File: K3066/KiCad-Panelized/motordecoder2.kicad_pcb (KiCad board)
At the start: 2 copper layers, 76 x 98 mm, 600 parts, among them J11 PAD, J12 PAD, J14 PAD, J16 PAD, J18 PAD, J19 PAD, P1 PAD, P10 PAD, P11 PAD, P2 PAD, P3 PAD, P4 PAD, P5 PAD, P6 PAD, P7 PAD, P8 PAD, P9 PROG, Q1 DMG6601LVT, Q11 SSM3K7002BFU, Q12 SSM6N7002BFE, Q13 SSM6N7002BFE, Q14 SSM6N7002BFE, Q2 DMG6601LVT, Q21 PMBT3906VS, Q22 SSM6N7002BFE, Q3 PMBT3904VS, Q5 2SC4116, Q6 PMBT3906VS, Q8 PMBT3904VS, U2 ATtiny1606-M

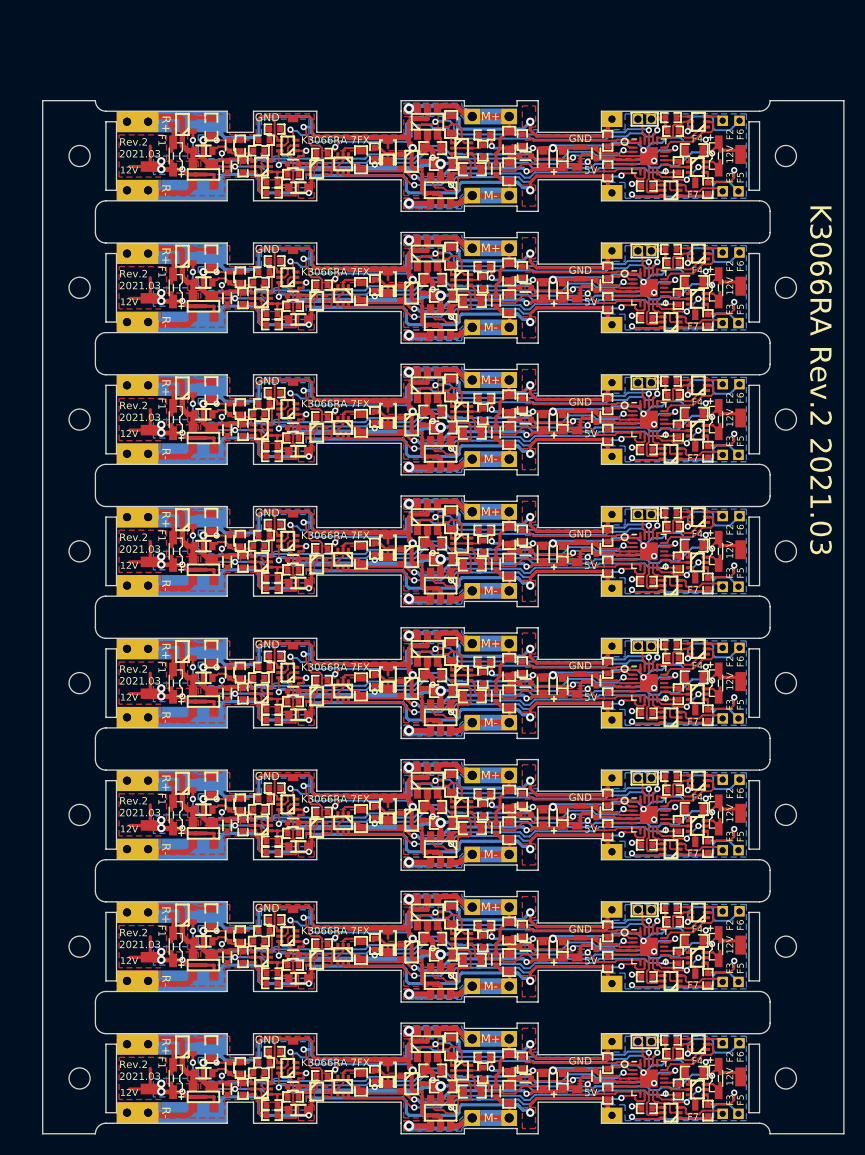
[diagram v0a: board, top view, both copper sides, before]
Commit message: 回路の問題点を修正 (K3066: Rev3 / それ以外: Rev2)
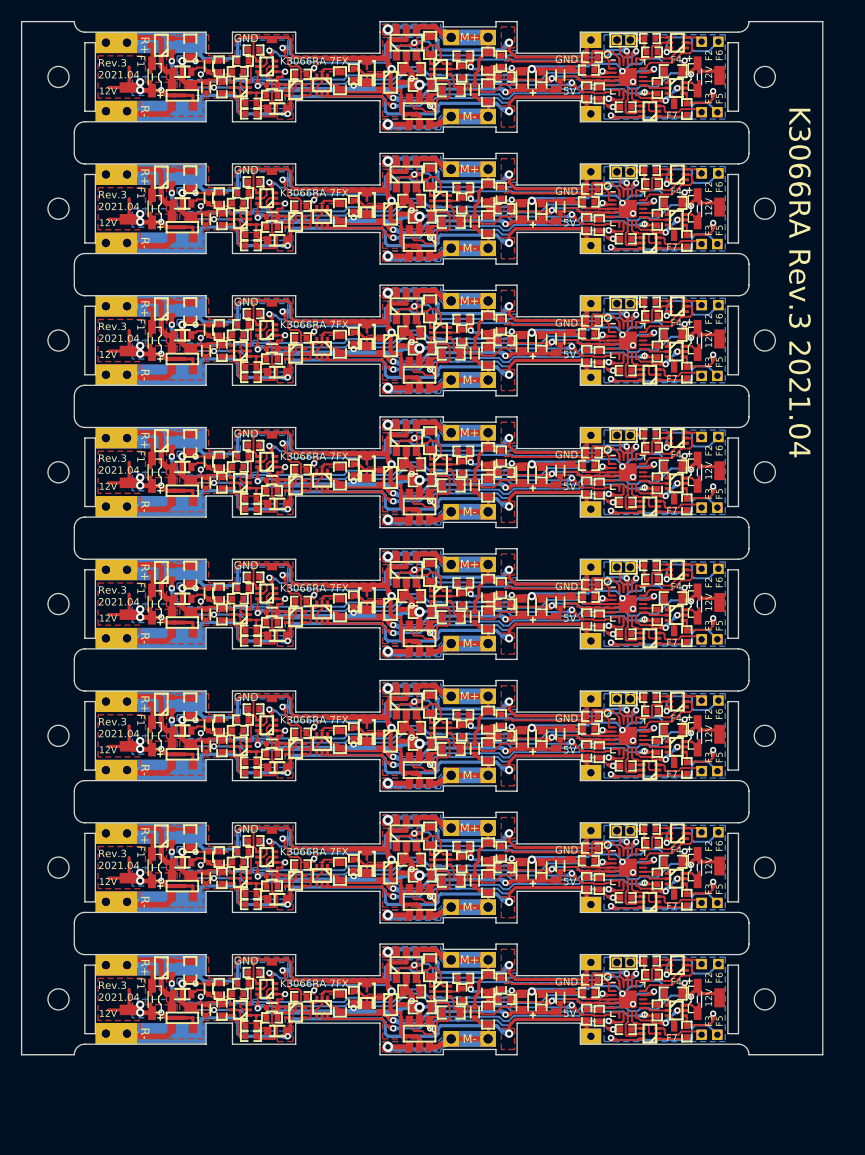
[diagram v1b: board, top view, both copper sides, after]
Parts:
- removed the C1 at (127.5, 138.8)
- removed the C1 at (127.5, 126.2)
- removed the C1 at (127.5, 113.8)
- removed the C1 at (127.5, 101.2)
- removed the C1 at (127.5, 88.8)
- removed the C1 at (127.5, 76.2)
- removed the C1 at (127.5, 63.8)
- removed the C11 at (127.8, 136.8)
- removed the C11 at (127.8, 124.2)
- removed the C11 at (127.8, 111.8)
- removed the C11 at (127.8, 99.2)
- removed the C11 at (127.8, 86.8)
- removed the C11 at (127.8, 74.2)
- removed the C11 at (127.8, 61.8)
- removed the C12 at (133.8, 138.5)
- removed the C12 at (133.8, 126.0)
- removed the C12 at (133.8, 113.5)
- removed the C12 at (133.8, 101.0)
- removed the C12 at (133.8, 88.5)
- removed the C12 at (133.8, 76.0)
- removed the C12 at (133.8, 63.5)
- removed the C3 at (157.5, 138.0)
- removed the C3 at (157.5, 125.5)
- removed the C3 at (157.5, 113.0)
- removed the C3 at (157.5, 100.5)
- removed the C3 at (157.5, 88.0)
- removed the C3 at (157.5, 75.5)
- removed the C3 at (157.5, 63.0)
- removed the C4 at (159.3, 138.0)
- removed the C4 at (159.3, 125.5)
- removed the C4 at (159.3, 113.0)
- removed the C4 at (159.3, 100.5)
- removed the C4 at (159.3, 88.0)
- removed the C4 at (159.3, 75.5)
- removed the C4 at (159.3, 63.0)
- removed the C5 at (162.5, 137.5)
- removed the C5 at (162.5, 125.0)
- removed the C5 at (162.5, 112.5)
- removed the C5 at (162.5, 100.0)
- removed the C5 at (162.5, 87.5)
- removed the C5 at (162.5, 75.0)
- removed the C5 at (162.5, 62.5)
- removed C6 (x8): 104, footprint:C_1005_v2
- removed the C7 at (153.0, 139.0)
- removed the C7 at (153.0, 126.5)
- removed the C7 at (153.0, 114.0)
- removed the C7 at (153.0, 101.5)
- removed the C7 at (153.0, 89.0)
- removed the C7 at (153.0, 76.5)
- removed the C7 at (153.0, 64.0)
- removed the D1 at (125.2, 139.5)
- removed the D1 at (125.2, 127.0)
- removed the D1 at (125.2, 114.5)
- removed the D1 at (125.2, 102.0)
- removed the D1 at (125.2, 89.5)
- removed the D1 at (125.2, 77.0)
- removed the D1 at (125.2, 64.5)
- removed the D11 at (122.0, 137.8)
- removed the D11 at (122.0, 125.2)
- removed the D11 at (122.0, 112.8)
- removed the D11 at (122.0, 100.2)
- removed the D11 at (122.0, 87.8)
- removed the D11 at (122.0, 75.2)
- removed the D11 at (122.0, 62.8)
- removed the D12 at (174.5, 137.8)
- removed the D12 at (174.5, 125.2)
- removed the D12 at (174.5, 112.8)
- removed the D12 at (174.5, 100.2)
- removed the D12 at (174.5, 87.8)
- removed the D12 at (174.5, 75.2)
- removed the D12 at (174.5, 62.8)
- removed the D21 at (125.2, 137.2)
- removed the D21 at (125.2, 124.8)
- removed the D21 at (125.2, 112.2)
- removed the D21 at (125.2, 99.8)
- removed the D21 at (125.2, 87.2)
- removed the D21 at (125.2, 74.8)
- removed the D21 at (125.2, 62.2)
- removed the D22 at (134.2, 140.8)
- removed the D22 at (134.2, 128.2)
- removed the D22 at (134.2, 115.8)
- removed the D22 at (134.2, 103.2)
- removed the D22 at (134.2, 90.8)
- removed the D22 at (134.2, 78.2)
- removed the D22 at (134.2, 65.8)
- removed the D3 at (142.8, 137.2)
- removed the D3 at (142.8, 124.8)
- removed the D3 at (142.8, 112.2)
- removed the D3 at (142.8, 99.8)
- removed the D3 at (142.8, 87.2)
- removed the D3 at (142.8, 74.8)
- removed the D3 at (142.8, 62.2)
- removed the J11 at (176.2, 137.6)
- removed the J11 at (176.2, 125.1)
- removed the J11 at (176.2, 112.6)
- removed the J11 at (176.2, 100.1)
- removed the J11 at (176.2, 87.6)
- removed the J11 at (176.2, 75.1)
- removed the J11 at (176.2, 62.6)
- removed the J12 at (176.0, 141.1)
- removed the J12 at (176.0, 128.6)
- removed the J12 at (176.0, 116.1)
- removed the J12 at (176.0, 103.6)
- removed the J12 at (176.0, 91.1)
- removed the J12 at (176.0, 78.6)
- removed the J12 at (176.0, 66.1)
- removed the J14 at (174.5, 141.1)
- removed the J14 at (174.5, 128.6)
- removed the J14 at (174.5, 116.1)
- removed the J14 at (174.5, 103.6)
- removed the J14 at (174.5, 91.1)
- removed the J14 at (174.5, 78.6)
- removed the J14 at (174.5, 66.1)
- removed the J16 at (176.1, 134.4)
- removed the J16 at (176.1, 121.9)
- removed the J16 at (176.1, 109.4)
- removed the J16 at (176.1, 96.9)
- removed the J16 at (176.1, 84.4)
- removed the J16 at (176.1, 71.9)
- removed the J16 at (176.1, 59.4)
- removed the J18 at (174.5, 134.4)
- removed the J18 at (174.5, 121.9)
- removed the J18 at (174.5, 109.4)
- removed the J18 at (174.5, 96.9)
- removed the J18 at (174.5, 84.4)
- removed the J18 at (174.5, 71.9)
- removed the J18 at (174.5, 59.4)
- removed the J19 at (171.9, 140.3)
- removed the J19 at (171.9, 127.8)
- removed the J19 at (171.9, 115.3)
- removed the J19 at (171.9, 102.8)
- removed the J19 at (171.9, 90.3)
- removed the J19 at (171.9, 77.8)
- removed the J19 at (171.9, 65.3)
- removed the P1 at (119.0, 134.5)
- removed the P1 at (119.0, 122.0)
- removed the P1 at (119.0, 109.5)
- removed the P1 at (119.0, 97.0)
- removed the P1 at (119.0, 84.5)
- removed the P1 at (119.0, 72.0)
- removed the P1 at (119.0, 59.5)
- removed the P10 at (160.7, 138.8)
- removed the P10 at (160.7, 126.3)
- removed the P10 at (160.7, 113.8)
- removed the P10 at (160.7, 101.3)
- removed the P10 at (160.7, 88.8)
- removed the P10 at (160.7, 76.3)
- removed the P10 at (160.7, 63.9)
- removed the P11 at (161.0, 136.9)
- removed the P11 at (161.0, 124.4)
- removed the P11 at (161.0, 111.9)
- removed the P11 at (161.0, 99.4)
- removed the P11 at (161.0, 86.9)
- removed the P11 at (161.0, 74.4)
- removed the P11 at (161.0, 61.9)
- removed the P11 at (161.0, 49.4)
- removed the P2 at (164.0, 134.2)
- removed the P2 at (164.0, 121.8)
- removed the P2 at (164.0, 109.2)
- removed the P2 at (164.0, 96.8)
- removed the P2 at (164.0, 84.2)
- removed the P2 at (164.0, 71.8)
- removed the P2 at (164.0, 59.2)
- removed the P3 at (119.0, 141.0)
- removed the P3 at (119.0, 128.5)
- removed the P3 at (119.0, 116.0)
- removed the P3 at (119.0, 103.5)
- removed the P3 at (119.0, 91.0)
- removed the P3 at (119.0, 78.5)
- removed the P3 at (119.0, 66.0)
- removed the P4 at (164.0, 141.2)
- removed the P4 at (164.0, 128.8)
- removed the P4 at (164.0, 116.2)
- removed the P4 at (164.0, 103.8)
- removed the P4 at (164.0, 91.2)
- removed the P4 at (164.0, 78.8)
- removed the P4 at (164.0, 66.2)
- removed the P5 at (152.5, 134.0)
- removed the P5 at (152.5, 121.5)
- removed the P5 at (152.5, 109.0)
- removed the P5 at (152.5, 96.5)
- removed the P5 at (152.5, 84.0)
- removed the P5 at (152.5, 71.5)
- removed the P5 at (152.5, 59.0)
- removed the P6 at (152.5, 141.5)
- removed the P6 at (152.5, 129.0)
- removed the P6 at (152.5, 116.5)
- removed the P6 at (152.5, 104.0)
- removed the P6 at (152.5, 91.5)
- removed the P6 at (152.5, 79.0)
- removed the P6 at (152.5, 66.5)
- removed the P7 at (120.2, 138.8)
- removed the P7 at (120.2, 126.2)
- removed the P7 at (120.2, 113.8)
- removed the P7 at (120.2, 101.2)
- removed the P7 at (120.2, 88.8)
- removed the P7 at (120.2, 76.2)
- removed the P7 at (120.2, 63.8)
- removed the P8 at (133.8, 134.2)
- removed the P8 at (133.8, 121.8)
- removed the P8 at (133.8, 109.2)
- removed the P8 at (133.8, 96.8)
- removed the P8 at (133.8, 84.2)
- removed the P8 at (133.8, 71.8)
- removed the P8 at (133.8, 59.2)
- removed the P9 at (167.1, 134.2)
- removed the P9 at (167.1, 121.8)
- removed the P9 at (167.1, 109.2)
- removed the P9 at (167.1, 96.8)
- removed the P9 at (167.1, 84.2)
- removed the P9 at (167.1, 71.8)
- removed the P9 at (167.1, 59.2)
- removed the Q1 at (146.5, 134.5)
- removed the Q1 at (146.5, 122.0)
- removed the Q1 at (146.5, 109.5)
- removed the Q1 at (146.5, 97.0)
- removed the Q1 at (146.5, 84.5)
- removed the Q1 at (146.5, 72.0)
- removed the Q1 at (146.5, 59.5)
- removed the Q11 at (123.2, 134.8)
- removed the Q11 at (123.2, 122.2)
- removed the Q11 at (123.2, 109.8)
- removed the Q11 at (123.2, 97.2)
- removed the Q11 at (123.2, 84.8)
- removed the Q11 at (123.2, 72.2)
- removed the Q11 at (123.2, 59.8)
- removed the Q12 at (172.1, 138.8)
- removed the Q12 at (172.1, 126.3)
- removed the Q12 at (172.1, 113.8)
- removed the Q12 at (172.1, 101.3)
- removed the Q12 at (172.1, 88.8)
- removed the Q12 at (172.1, 76.3)
- removed the Q12 at (172.1, 63.8)
- removed the Q13 at (169.6, 141.0)
- removed the Q13 at (169.6, 128.5)
- removed the Q13 at (169.6, 116.0)
- removed the Q13 at (169.6, 103.5)
- removed the Q13 at (169.6, 91.0)
- removed the Q13 at (169.6, 78.5)
- removed the Q13 at (169.6, 66.0)
- removed the Q14 at (172.2, 134.5)
- removed the Q14 at (172.2, 122.0)
- removed the Q14 at (172.2, 109.5)
- removed the Q14 at (172.2, 97.0)
- removed the Q14 at (172.2, 84.5)
- removed the Q14 at (172.2, 72.0)
- removed the Q14 at (172.2, 59.5)
- removed the Q2 at (147.8, 141.0)
- removed the Q2 at (147.8, 128.5)
- removed the Q2 at (147.8, 116.0)
- removed the Q2 at (147.8, 103.5)
- removed the Q2 at (147.8, 91.0)
- removed the Q2 at (147.8, 78.5)
- removed the Q2 at (147.8, 66.0)
- removed the Q21 at (130.8, 138.8)
- removed the Q21 at (130.8, 126.2)
- removed the Q21 at (130.8, 113.8)
- removed the Q21 at (130.8, 101.2)
- removed the Q21 at (130.8, 88.8)
- removed the Q21 at (130.8, 76.2)
- removed the Q21 at (130.8, 63.8)
- removed the Q22 at (133.2, 136.8)
- removed the Q22 at (133.2, 124.2)
- removed the Q22 at (133.2, 111.8)
- removed the Q22 at (133.2, 99.2)
- removed the Q22 at (133.2, 86.8)
- removed the Q22 at (133.2, 74.2)
- removed the Q22 at (133.2, 61.8)
- removed the Q3 at (149.8, 137.0)
- removed the Q3 at (149.8, 124.5)
- removed the Q3 at (149.8, 112.0)
- removed the Q3 at (149.8, 99.5)
- removed the Q3 at (149.8, 87.0)
- removed the Q3 at (149.8, 74.5)
- removed the Q3 at (149.8, 62.0)
- removed the Q5 at (145.0, 138.2)
- removed the Q5 at (145.0, 125.8)
- removed the Q5 at (145.0, 113.2)
- removed the Q5 at (145.0, 100.8)
- removed the Q5 at (145.0, 88.2)
- removed the Q5 at (145.0, 75.8)
- removed the Q5 at (145.0, 63.2)
- removed the Q6 at (138.5, 138.5)
- removed the Q6 at (138.5, 126.0)
- removed the Q6 at (138.5, 113.5)
- removed the Q6 at (138.5, 101.0)
- removed the Q6 at (138.5, 88.5)
- removed the Q6 at (138.5, 76.0)
- removed the Q6 at (138.5, 63.5)
- removed the Q8 at (136.0, 139.0)
- removed the Q8 at (136.0, 126.5)
- removed the Q8 at (136.0, 114.0)
- removed the Q8 at (136.0, 101.5)
- removed the Q8 at (136.0, 89.0)
- removed the Q8 at (136.0, 76.5)
- removed the Q8 at (136.0, 64.0)
- removed the R1 at (163.6, 136.3)
- removed the R1 at (163.6, 123.8)
- removed the R1 at (163.6, 111.3)
- removed the R1 at (163.6, 98.8)
- removed the R1 at (163.6, 86.3)
- removed the R1 at (163.6, 73.8)
- removed the R1 at (163.6, 61.3)
- removed the R1 at (163.6, 48.8)
- removed the R10 at (154.2, 139.2)
- removed the R10 at (154.2, 126.8)
- removed the R10 at (154.2, 114.2)
- removed the R10 at (154.2, 101.8)
- removed the R10 at (154.2, 89.2)
- removed the R10 at (154.2, 76.8)
- removed the R10 at (154.2, 64.2)
- removed the R11 at (155.5, 136.2)
- removed the R11 at (155.5, 123.8)
- removed the R11 at (155.5, 111.2)
- removed the R11 at (155.5, 98.8)
- removed the R11 at (155.5, 86.2)
- removed the R11 at (155.5, 73.8)
- removed the R11 at (155.5, 61.2)
- removed the R12 at (141.5, 137.5)
- removed the R12 at (141.5, 125.0)
- removed the R12 at (141.5, 112.5)
- removed the R12 at (141.5, 100.0)
- removed the R12 at (141.5, 87.5)
- removed the R12 at (141.5, 75.0)
- removed the R12 at (141.5, 62.5)
- removed the R13 at (170.3, 138.8)
- removed the R13 at (170.3, 126.3)
- removed the R13 at (170.3, 113.8)
- removed the R13 at (170.3, 101.3)
- removed the R13 at (170.3, 88.8)
- removed the R13 at (170.3, 76.3)
- removed the R13 at (170.3, 63.8)
- removed the R14 at (140.2, 138.1)
- removed the R14 at (140.2, 125.6)
- removed the R14 at (140.2, 113.1)
- removed the R14 at (140.2, 100.6)
- removed the R14 at (140.2, 88.1)
- removed the R14 at (140.2, 75.6)
- removed the R14 at (140.2, 63.1)
- removed the R15 at (136.5, 137.5)
- removed the R15 at (136.5, 125.0)
- removed the R15 at (136.5, 112.5)
- removed the R15 at (136.5, 100.0)
- removed the R15 at (136.5, 87.5)
- removed the R15 at (136.5, 75.0)
- removed the R15 at (136.5, 62.5)
- removed the R2 at (163.6, 139.2)
- removed the R2 at (163.6, 126.7)
- removed the R2 at (163.6, 114.2)
- removed the R2 at (163.6, 101.7)
- removed the R2 at (163.6, 89.2)
- removed the R2 at (163.6, 76.7)
- removed the R2 at (163.6, 64.2)
- removed the R21 at (126.0, 135.0)
- removed the R21 at (126.0, 122.5)
- removed the R21 at (126.0, 110.0)
- removed the R21 at (126.0, 97.5)
- removed the R21 at (126.0, 85.0)
- removed the R21 at (126.0, 72.5)
- removed the R21 at (126.0, 60.0)
- removed the R22 at (171.8, 137.2)
- removed the R22 at (171.8, 124.7)
- removed the R22 at (171.8, 112.2)
- removed the R22 at (171.8, 99.7)
- removed the R22 at (171.8, 87.2)
- removed the R22 at (171.8, 74.7)
- removed the R22 at (171.8, 62.2)
- removed the R23 at (173.1, 140.8)
- removed the R23 at (173.1, 128.3)
- removed the R23 at (173.1, 115.8)
- removed the R23 at (173.1, 103.3)
- removed the R23 at (173.1, 90.8)
- removed the R23 at (173.1, 78.3)
- removed the R23 at (173.1, 65.8)
- removed the R24 at (167.3, 140.6)
- removed the R24 at (167.3, 128.1)
- removed the R24 at (167.3, 115.6)
- removed the R24 at (167.3, 103.1)
- removed the R24 at (167.3, 90.6)
- removed the R24 at (167.3, 78.1)
- removed the R24 at (167.3, 65.6)
- removed the R25 at (169.8, 135.4)
- removed the R25 at (169.8, 122.9)
- removed the R25 at (169.8, 110.4)
- removed the R25 at (169.8, 97.9)
- removed the R25 at (169.8, 85.4)
- removed the R25 at (169.8, 72.9)
- removed the R25 at (169.8, 60.4)
- removed the R26 at (169.6, 134.1)
- removed the R26 at (169.6, 121.6)
- removed the R26 at (169.6, 109.1)
- removed the R26 at (169.6, 96.6)
- removed the R26 at (169.6, 84.1)
- removed the R26 at (169.6, 71.6)
- removed the R26 at (169.6, 59.1)
- removed the R3 at (147.0, 137.0)
- removed the R3 at (147.0, 124.5)
- removed the R3 at (147.0, 112.0)
- removed the R3 at (147.0, 99.5)
- removed the R3 at (147.0, 87.0)
- removed the R3 at (147.0, 74.5)
- removed the R3 at (147.0, 62.0)
- removed the R31 at (130.5, 137.2)
- removed the R31 at (130.5, 124.8)
- removed the R31 at (130.5, 112.2)
- removed the R31 at (130.5, 99.8)
- removed the R31 at (130.5, 87.2)
- removed the R31 at (130.5, 74.8)
- removed the R31 at (130.5, 62.2)
- removed the R32 at (128.8, 136.8)
- removed the R32 at (128.8, 124.2)
- removed the R32 at (128.8, 111.8)
- removed the R32 at (128.8, 99.2)
- removed the R32 at (128.8, 86.8)
- removed the R32 at (128.8, 74.2)
- removed the R32 at (128.8, 61.8)
- removed the R33 at (129.0, 138.8)
- removed the R33 at (129.0, 126.2)
- removed the R33 at (129.0, 113.8)
- removed the R33 at (129.0, 101.2)
- removed the R33 at (129.0, 88.8)
- removed the R33 at (129.0, 76.2)
- removed the R33 at (129.0, 63.8)
- removed the R34 at (131.8, 141.2)
- removed the R34 at (131.8, 128.8)
- removed the R34 at (131.8, 116.2)
- removed the R34 at (131.8, 103.8)
- removed the R34 at (131.8, 91.2)
- removed the R34 at (131.8, 78.8)
- removed the R34 at (131.8, 66.2)
- removed the R35 at (131.8, 140.2)
- removed the R35 at (131.8, 127.8)
- removed the R35 at (131.8, 115.2)
- removed the R35 at (131.8, 102.8)
- removed the R35 at (131.8, 90.2)
- removed the R35 at (131.8, 77.8)
- removed the R35 at (131.8, 65.2)
- removed the R36 at (133.8, 139.5)
- removed the R36 at (133.8, 127.0)
- removed the R36 at (133.8, 114.5)
- removed the R36 at (133.8, 102.0)
- removed the R36 at (133.8, 89.5)
- removed the R36 at (133.8, 77.0)
- removed the R36 at (133.8, 64.5)
- removed the R37 at (131.0, 136.2)
- removed the R37 at (131.0, 123.8)
- removed the R37 at (131.0, 111.2)
- removed the R37 at (131.0, 98.8)
- removed the R37 at (131.0, 86.2)
- removed the R37 at (131.0, 73.8)
- removed the R37 at (131.0, 61.2)
- removed the R38 at (132.0, 135.2)
- removed the R38 at (132.0, 122.7)
- removed the R38 at (132.0, 110.2)
- removed the R38 at (132.0, 97.7)
- removed the R38 at (132.0, 85.2)
- removed the R38 at (132.0, 72.7)
- removed the R38 at (132.0, 60.2)
- removed the R4 at (148.0, 138.5)
- removed the R4 at (148.0, 126.0)
- removed the R4 at (148.0, 113.5)
- removed the R4 at (148.0, 101.0)
- removed the R4 at (148.0, 88.5)
- removed the R4 at (148.0, 76.0)
- removed the R4 at (148.0, 63.5)
- removed the R5 at (148.8, 134.8)
- removed the R5 at (148.8, 122.2)
- removed the R5 at (148.8, 109.8)
- removed the R5 at (148.8, 97.2)
- removed the R5 at (148.8, 84.8)
- removed the R5 at (148.8, 72.2)
- removed the R5 at (148.8, 59.8)
- removed the R6 at (150.8, 139.0)
- removed the R6 at (150.8, 126.5)
- removed the R6 at (150.8, 114.0)
- removed the R6 at (150.8, 101.5)
- removed the R6 at (150.8, 89.0)
- removed the R6 at (150.8, 76.5)
- removed the R6 at (150.8, 64.0)
- removed the R7 at (151.8, 137.2)
- removed the R7 at (151.8, 124.8)
- removed the R7 at (151.8, 112.2)
- removed the R7 at (151.8, 99.8)
- removed the R7 at (151.8, 87.2)
- removed the R7 at (151.8, 74.8)
- removed the R7 at (151.8, 62.2)
- removed the R8 at (151.9, 135.8)
- removed the R8 at (151.9, 123.2)
- removed the R8 at (151.9, 110.8)
- removed the R8 at (151.9, 98.2)
- removed the R8 at (151.9, 85.8)
- removed the R8 at (151.9, 73.2)
- removed the R8 at (151.9, 60.8)
- removed the R9 at (154.2, 136.2)
- removed the R9 at (154.2, 123.8)
- removed the R9 at (154.2, 111.2)
- removed the R9 at (154.2, 98.8)
- removed the R9 at (154.2, 86.2)
- removed the R9 at (154.2, 73.8)
- removed the R9 at (154.2, 61.2)
- removed the REF** at (113.5, 137.8)
- removed the REF** at (180.5, 112.8)
- removed the REF** at (180.5, 100.2)
- removed the REF** at (180.5, 87.8)
- removed the REF** at (180.5, 75.2)
- removed the REF** at (180.5, 62.8)
- removed the REF** at (180.5, 50.2)
- removed the REF** at (113.5, 50.2)
- removed the REF** at (113.5, 125.2)
- removed the REF** at (113.5, 112.8)
- removed the REF** at (113.5, 100.2)
- removed the REF** at (113.5, 87.8)
- removed the REF** at (113.5, 75.2)
- removed the REF** at (113.5, 62.8)
- removed the REF** at (180.5, 137.8)
- removed the REF** at (180.5, 125.2)
- removed the U2 at (167.5, 137.8)
- removed the U2 at (167.5, 125.2)
- removed the U2 at (167.5, 112.8)
- removed the U2 at (167.5, 100.2)
- removed the U2 at (167.5, 87.8)
- removed the U2 at (167.5, 75.2)
- removed the U2 at (167.5, 62.8)
- added C1: 104, footprint:C_1005_v2, F.Cu at (125.5, 131.2)
- added C1: 104, footprint:C_1005_v2, F.Cu at (125.5, 118.8)
- added C1: 104, footprint:C_1005_v2, F.Cu at (125.5, 106.2)
- added C1: 104, footprint:C_1005_v2, F.Cu at (125.5, 93.8)
- added C1: 104, footprint:C_1005_v2, F.Cu at (125.5, 81.2)
- added C1: 104, footprint:C_1005_v2, F.Cu at (125.5, 68.8)
- added C1: 104, footprint:C_1005_v2, F.Cu at (125.5, 56.2)
- added C11: 105, footprint:C_1005_v2, F.Cu at (125.8, 129.2)
- added C11: 105, footprint:C_1005_v2, F.Cu at (125.8, 116.8)
- added C11: 105, footprint:C_1005_v2, F.Cu at (125.8, 104.2)
- added C11: 105, footprint:C_1005_v2, F.Cu at (125.8, 91.8)
- added C11: 105, footprint:C_1005_v2, F.Cu at (125.8, 79.2)
- added C11: 105, footprint:C_1005_v2, F.Cu at (125.8, 66.8)
- added C11: 105, footprint:C_1005_v2, F.Cu at (125.8, 54.2)
- added C12: 105, footprint:C_1005_v2, F.Cu at (131.8, 131.0)
- added C12: 105, footprint:C_1005_v2, F.Cu at (131.8, 118.5)
- added C12: 105, footprint:C_1005_v2, F.Cu at (131.8, 106.0)
- added C12: 105, footprint:C_1005_v2, F.Cu at (131.8, 93.5)
- added C12: 105, footprint:C_1005_v2, F.Cu at (131.8, 81.0)
- added C12: 105, footprint:C_1005_v2, F.Cu at (131.8, 68.5)
- added C12: 105, footprint:C_1005_v2, F.Cu at (131.8, 56.0)
- added C3: 226, footprint:C_1608, F.Cu at (155.5, 130.5)
- added C3: 226, footprint:C_1608, F.Cu at (155.5, 118.0)
- added C3: 226, footprint:C_1608, F.Cu at (155.5, 105.5)
- added C3: 226, footprint:C_1608, F.Cu at (155.5, 93.0)
- added C3: 226, footprint:C_1608, F.Cu at (155.5, 80.5)
- added C3: 226, footprint:C_1608, F.Cu at (155.5, 68.0)
- added C3: 226, footprint:C_1608, F.Cu at (155.5, 55.5)
- added C4: 476, footprint:CP_1608, F.Cu at (157.3, 130.5)
- added C4: 476, footprint:CP_1608, F.Cu at (157.3, 118.0)
- added C4: 476, footprint:CP_1608, F.Cu at (157.3, 105.5)
- added C4: 476, footprint:CP_1608, F.Cu at (157.3, 93.0)
- added C4: 476, footprint:CP_1608, F.Cu at (157.3, 80.5)
- added C4: 476, footprint:CP_1608, F.Cu at (157.3, 68.0)
- added C4: 476, footprint:CP_1608, F.Cu at (157.3, 55.5)
- added C5: 104, footprint:C_1005_v2, F.Cu at (159.1, 130.1)
- added C5: 104, footprint:C_1005_v2, F.Cu at (159.1, 117.6)
- added C5: 104, footprint:C_1005_v2, F.Cu at (159.1, 105.1)
- added C5: 104, footprint:C_1005_v2, F.Cu at (159.1, 92.6)
- added C5: 104, footprint:C_1005_v2, F.Cu at (159.1, 80.1)
- added C5: 104, footprint:C_1005_v2, F.Cu at (159.1, 67.6)
- added C5: 104, footprint:C_1005_v2, F.Cu at (159.1, 55.1)
- added C7: 182, footprint:C_1005_v2, F.Cu at (151.0, 131.5)
- added C7: 182, footprint:C_1005_v2, F.Cu at (151.0, 119.0)
- added C7: 182, footprint:C_1005_v2, F.Cu at (151.0, 106.5)
- added C7: 182, footprint:C_1005_v2, F.Cu at (151.0, 94.0)
- added C7: 182, footprint:C_1005_v2, F.Cu at (151.0, 81.5)
- added C7: 182, footprint:C_1005_v2, F.Cu at (151.0, 69.0)
- added C7: 182, footprint:C_1005_v2, F.Cu at (151.0, 56.5)
- added D1: BAS3007, footprint:SOT-143, F.Cu at (123.2, 132.0)
- added D1: BAS3007, footprint:SOT-143, F.Cu at (123.2, 119.5)
- added D1: BAS3007, footprint:SOT-143, F.Cu at (123.2, 107.0)
- added D1: BAS3007, footprint:SOT-143, F.Cu at (123.2, 94.5)
- added D1: BAS3007, footprint:SOT-143, F.Cu at (123.2, 82.0)
- added D1: BAS3007, footprint:SOT-143, F.Cu at (123.2, 69.5)
- added D1: BAS3007, footprint:SOT-143, F.Cu at (123.2, 57.0)
- added D11: LED, footprint:LED_1224_1005_SIDE, F.Cu at (120.0, 130.2)
- added D11: LED, footprint:LED_1224_1005_SIDE, F.Cu at (120.0, 117.8)
- added D11: LED, footprint:LED_1224_1005_SIDE, F.Cu at (120.0, 105.2)
- added D11: LED, footprint:LED_1224_1005_SIDE, F.Cu at (120.0, 92.8)
- added D11: LED, footprint:LED_1224_1005_SIDE, F.Cu at (120.0, 80.2)
- added D11: LED, footprint:LED_1224_1005_SIDE, F.Cu at (120.0, 67.8)
- added D11: LED, footprint:LED_1224_1005_SIDE, F.Cu at (120.0, 55.2)
- added D12: LED, footprint:LED_1224_1005_SIDE, F.Cu at (172.5, 130.2)
- added D12: LED, footprint:LED_1224_1005_SIDE, F.Cu at (172.5, 117.8)
- added D12: LED, footprint:LED_1224_1005_SIDE, F.Cu at (172.5, 105.2)
- added D12: LED, footprint:LED_1224_1005_SIDE, F.Cu at (172.5, 92.8)
- added D12: LED, footprint:LED_1224_1005_SIDE, F.Cu at (172.5, 80.2)
- added D12: LED, footprint:LED_1224_1005_SIDE, F.Cu at (172.5, 67.8)
- added D12: LED, footprint:LED_1224_1005_SIDE, F.Cu at (172.5, 55.2)
- added D21: BAT43XV2, footprint:EMD2_small, F.Cu at (123.2, 129.8)
- added D21: BAT43XV2, footprint:EMD2_small, F.Cu at (123.2, 117.2)
- added D21: BAT43XV2, footprint:EMD2_small, F.Cu at (123.2, 104.8)
- added D21: BAT43XV2, footprint:EMD2_small, F.Cu at (123.2, 92.2)
- added D21: BAT43XV2, footprint:EMD2_small, F.Cu at (123.2, 79.8)
- added D21: BAT43XV2, footprint:EMD2_small, F.Cu at (123.2, 67.2)
- added D21: BAT43XV2, footprint:EMD2_small, F.Cu at (123.2, 54.8)
- added D22: BAT43XV2, footprint:EMD2, F.Cu at (132.2, 133.2)
- added D22: BAT43XV2, footprint:EMD2, F.Cu at (132.2, 120.8)
- added D22: BAT43XV2, footprint:EMD2, F.Cu at (132.2, 108.2)
- added D22: BAT43XV2, footprint:EMD2, F.Cu at (132.2, 95.8)
- added D22: BAT43XV2, footprint:EMD2, F.Cu at (132.2, 83.2)
- added D22: BAT43XV2, footprint:EMD2, F.Cu at (132.2, 70.8)
- added D22: BAT43XV2, footprint:EMD2, F.Cu at (132.2, 58.2)
- added D3: UDZV5.6B, footprint:UMD2, F.Cu at (140.8, 129.8)
- added D3: UDZV5.6B, footprint:UMD2, F.Cu at (140.8, 117.2)
- added D3: UDZV5.6B, footprint:UMD2, F.Cu at (140.8, 104.8)
- added D3: UDZV5.6B, footprint:UMD2, F.Cu at (140.8, 92.2)
- added D3: UDZV5.6B, footprint:UMD2, F.Cu at (140.8, 79.8)
- added D3: UDZV5.6B, footprint:UMD2, F.Cu at (140.8, 67.2)
- added D3: UDZV5.6B, footprint:UMD2, F.Cu at (140.8, 54.8)
- added J11: PAD, footprint:PAD_1.0x1.8_SMD, F.Cu at (174.2, 130.1)
- added J11: PAD, footprint:PAD_1.0x1.8_SMD, F.Cu at (174.2, 117.6)
- added J11: PAD, footprint:PAD_1.0x1.8_SMD, F.Cu at (174.2, 105.1)
- added J11: PAD, footprint:PAD_1.0x1.8_SMD, F.Cu at (174.2, 92.6)
- added J11: PAD, footprint:PAD_1.0x1.8_SMD, F.Cu at (174.2, 80.1)
- added J11: PAD, footprint:PAD_1.0x1.8_SMD, F.Cu at (174.2, 67.6)
- added J11: PAD, footprint:PAD_1.0x1.8_SMD, F.Cu at (174.2, 55.1)
- added J12: PAD, footprint:PAD_1.0x1.0_Hole0.6, F.Cu at (174.0, 133.6)
- added J12: PAD, footprint:PAD_1.0x1.0_Hole0.6, F.Cu at (174.0, 121.1)
- added J12: PAD, footprint:PAD_1.0x1.0_Hole0.6, F.Cu at (174.0, 108.6)
- added J12: PAD, footprint:PAD_1.0x1.0_Hole0.6, F.Cu at (174.0, 96.1)
- added J12: PAD, footprint:PAD_1.0x1.0_Hole0.6, F.Cu at (174.0, 83.6)
- added J12: PAD, footprint:PAD_1.0x1.0_Hole0.6, F.Cu at (174.0, 71.1)
- added J12: PAD, footprint:PAD_1.0x1.0_Hole0.6, F.Cu at (174.0, 58.6)
- added J14: PAD, footprint:PAD_1.0x1.0_Hole0.6, F.Cu at (172.5, 133.6)
- added J14: PAD, footprint:PAD_1.0x1.0_Hole0.6, F.Cu at (172.5, 121.1)
- added J14: PAD, footprint:PAD_1.0x1.0_Hole0.6, F.Cu at (172.5, 108.6)
- added J14: PAD, footprint:PAD_1.0x1.0_Hole0.6, F.Cu at (172.5, 96.1)
- added J14: PAD, footprint:PAD_1.0x1.0_Hole0.6, F.Cu at (172.5, 83.6)
- added J14: PAD, footprint:PAD_1.0x1.0_Hole0.6, F.Cu at (172.5, 71.1)
- added J14: PAD, footprint:PAD_1.0x1.0_Hole0.6, F.Cu at (172.5, 58.6)
- added J16: PAD, footprint:PAD_1.0x1.0_Hole0.6, F.Cu at (174.1, 126.9)
- added J16: PAD, footprint:PAD_1.0x1.0_Hole0.6, F.Cu at (174.1, 114.4)
- added J16: PAD, footprint:PAD_1.0x1.0_Hole0.6, F.Cu at (174.1, 101.9)
- added J16: PAD, footprint:PAD_1.0x1.0_Hole0.6, F.Cu at (174.1, 89.4)
- added J16: PAD, footprint:PAD_1.0x1.0_Hole0.6, F.Cu at (174.1, 76.9)
- added J16: PAD, footprint:PAD_1.0x1.0_Hole0.6, F.Cu at (174.1, 64.4)
- added J16: PAD, footprint:PAD_1.0x1.0_Hole0.6, F.Cu at (174.1, 51.9)
- added J18: PAD, footprint:PAD_1.0x1.0_Hole0.6, F.Cu at (172.5, 126.9)
- added J18: PAD, footprint:PAD_1.0x1.0_Hole0.6, F.Cu at (172.5, 114.4)
- added J18: PAD, footprint:PAD_1.0x1.0_Hole0.6, F.Cu at (172.5, 101.9)
- added J18: PAD, footprint:PAD_1.0x1.0_Hole0.6, F.Cu at (172.5, 89.4)
- added J18: PAD, footprint:PAD_1.0x1.0_Hole0.6, F.Cu at (172.5, 76.9)
- added J18: PAD, footprint:PAD_1.0x1.0_Hole0.6, F.Cu at (172.5, 64.4)
- added J18: PAD, footprint:PAD_1.0x1.0_Hole0.6, F.Cu at (172.5, 51.9)
- added J19: PAD, footprint:PAD_0.6x1.0_SMD, F.Cu at (169.9, 132.8)
- added J19: PAD, footprint:PAD_0.6x1.0_SMD, F.Cu at (169.9, 120.3)
- added J19: PAD, footprint:PAD_0.6x1.0_SMD, F.Cu at (169.9, 107.8)
- added J19: PAD, footprint:PAD_0.6x1.0_SMD, F.Cu at (169.9, 95.3)
- added J19: PAD, footprint:PAD_0.6x1.0_SMD, F.Cu at (169.9, 82.8)
- added J19: PAD, footprint:PAD_0.6x1.0_SMD, F.Cu at (169.9, 70.3)
- added J19: PAD, footprint:PAD_0.6x1.0_SMD, F.Cu at (169.9, 57.8)
- added P1: PAD, footprint:KATO_FRAMEPAD_3066_v2, F.Cu at (117.0, 127.0)
- added P1: PAD, footprint:KATO_FRAMEPAD_3066_v2, F.Cu at (117.0, 114.5)
- added P1: PAD, footprint:KATO_FRAMEPAD_3066_v2, F.Cu at (117.0, 102.0)
- added P1: PAD, footprint:KATO_FRAMEPAD_3066_v2, F.Cu at (117.0, 89.5)
- added P1: PAD, footprint:KATO_FRAMEPAD_3066_v2, F.Cu at (117.0, 77.0)
- added P1: PAD, footprint:KATO_FRAMEPAD_3066_v2, F.Cu at (117.0, 64.5)
- added P1: PAD, footprint:KATO_FRAMEPAD_3066_v2, F.Cu at (117.0, 52.0)
- added P10: PAD, footprint:PAD_0.6x1.0_SMD, F.Cu at (158.7, 131.4)
- added P10: PAD, footprint:PAD_0.6x1.0_SMD, F.Cu at (158.7, 118.9)
- added P10: PAD, footprint:PAD_0.6x1.0_SMD, F.Cu at (158.7, 106.4)
- added P10: PAD, footprint:PAD_0.6x1.0_SMD, F.Cu at (158.7, 93.9)
- added P10: PAD, footprint:PAD_0.6x1.0_SMD, F.Cu at (158.7, 81.4)
- added P10: PAD, footprint:PAD_0.6x1.0_SMD, F.Cu at (158.7, 68.9)
- added P10: PAD, footprint:PAD_0.6x1.0_SMD, F.Cu at (158.7, 56.4)
- added P11: PAD, footprint:PAD_0.7x0.9_SMD, F.Cu at (160.1, 129.5)
- added P11: PAD, footprint:PAD_0.7x0.9_SMD, F.Cu at (160.1, 117.0)
- added P11: PAD, footprint:PAD_0.7x0.9_SMD, F.Cu at (160.1, 104.5)
- added P11: PAD, footprint:PAD_0.7x0.9_SMD, F.Cu at (160.1, 92.0)
- added P11: PAD, footprint:PAD_0.7x0.9_SMD, F.Cu at (160.1, 79.5)
- added P11: PAD, footprint:PAD_0.7x0.9_SMD, F.Cu at (160.1, 67.0)
- added P11: PAD, footprint:PAD_0.7x0.9_SMD, F.Cu at (160.1, 54.5)
- added P11: PAD, footprint:PAD_0.7x0.9_SMD, F.Cu at (160.1, 42.0)
- added P2: PAD, footprint:KATO_FRAMEPAD_3066_2, F.Cu at (162.0, 126.8)
- added P2: PAD, footprint:KATO_FRAMEPAD_3066_2, F.Cu at (162.0, 114.2)
- added P2: PAD, footprint:KATO_FRAMEPAD_3066_2, F.Cu at (162.0, 101.8)
- added P2: PAD, footprint:KATO_FRAMEPAD_3066_2, F.Cu at (162.0, 89.2)
- added P2: PAD, footprint:KATO_FRAMEPAD_3066_2, F.Cu at (162.0, 76.8)
- added P2: PAD, footprint:KATO_FRAMEPAD_3066_2, F.Cu at (162.0, 64.2)
- added P2: PAD, footprint:KATO_FRAMEPAD_3066_2, F.Cu at (162.0, 51.8)
- added P3: PAD, footprint:KATO_FRAMEPAD_3066_v2, F.Cu at (117.0, 133.5)
- added P3: PAD, footprint:KATO_FRAMEPAD_3066_v2, F.Cu at (117.0, 121.0)
- added P3: PAD, footprint:KATO_FRAMEPAD_3066_v2, F.Cu at (117.0, 108.5)
- added P3: PAD, footprint:KATO_FRAMEPAD_3066_v2, F.Cu at (117.0, 96.0)
- added P3: PAD, footprint:KATO_FRAMEPAD_3066_v2, F.Cu at (117.0, 83.5)
- added P3: PAD, footprint:KATO_FRAMEPAD_3066_v2, F.Cu at (117.0, 71.0)
- added P3: PAD, footprint:KATO_FRAMEPAD_3066_v2, F.Cu at (117.0, 58.5)
- added P4: PAD, footprint:KATO_FRAMEPAD_3066_2, F.Cu at (162.0, 133.8)
- added P4: PAD, footprint:KATO_FRAMEPAD_3066_2, F.Cu at (162.0, 121.2)
- added P4: PAD, footprint:KATO_FRAMEPAD_3066_2, F.Cu at (162.0, 108.8)
- added P4: PAD, footprint:KATO_FRAMEPAD_3066_2, F.Cu at (162.0, 96.2)
- added P4: PAD, footprint:KATO_FRAMEPAD_3066_2, F.Cu at (162.0, 83.8)
- added P4: PAD, footprint:KATO_FRAMEPAD_3066_2, F.Cu at (162.0, 71.2)
- added P4: PAD, footprint:KATO_FRAMEPAD_3066_2, F.Cu at (162.0, 58.8)
- added P5: PAD, footprint:KATO_MOTORPAD_3066, F.Cu at (150.5, 126.5)
- added P5: PAD, footprint:KATO_MOTORPAD_3066, F.Cu at (150.5, 114.0)
- added P5: PAD, footprint:KATO_MOTORPAD_3066, F.Cu at (150.5, 101.5)
- added P5: PAD, footprint:KATO_MOTORPAD_3066, F.Cu at (150.5, 89.0)
- added P5: PAD, footprint:KATO_MOTORPAD_3066, F.Cu at (150.5, 76.5)
- added P5: PAD, footprint:KATO_MOTORPAD_3066, F.Cu at (150.5, 64.0)
- added P5: PAD, footprint:KATO_MOTORPAD_3066, F.Cu at (150.5, 51.5)
- added P6: PAD, footprint:KATO_MOTORPAD_3066, F.Cu at (150.5, 134.0)
- added P6: PAD, footprint:KATO_MOTORPAD_3066, F.Cu at (150.5, 121.5)
- added P6: PAD, footprint:KATO_MOTORPAD_3066, F.Cu at (150.5, 109.0)
- added P6: PAD, footprint:KATO_MOTORPAD_3066, F.Cu at (150.5, 96.5)
- added P6: PAD, footprint:KATO_MOTORPAD_3066, F.Cu at (150.5, 84.0)
- added P6: PAD, footprint:KATO_MOTORPAD_3066, F.Cu at (150.5, 71.5)
- added P6: PAD, footprint:KATO_MOTORPAD_3066, F.Cu at (150.5, 59.0)
- added P7: PAD, footprint:PAD_1.0x1.8_SMD, F.Cu at (118.2, 131.2)
- added P7: PAD, footprint:PAD_1.0x1.8_SMD, F.Cu at (118.2, 118.8)
- added P7: PAD, footprint:PAD_1.0x1.8_SMD, F.Cu at (118.2, 106.2)
- added P7: PAD, footprint:PAD_1.0x1.8_SMD, F.Cu at (118.2, 93.8)
- added P7: PAD, footprint:PAD_1.0x1.8_SMD, F.Cu at (118.2, 81.2)
- added P7: PAD, footprint:PAD_1.0x1.8_SMD, F.Cu at (118.2, 68.8)
- added P7: PAD, footprint:PAD_1.0x1.8_SMD, F.Cu at (118.2, 56.2)
- added P8: PAD, footprint:PAD_0.6x1.0_SMD, F.Cu at (131.8, 126.8)
- added P8: PAD, footprint:PAD_0.6x1.0_SMD, F.Cu at (131.8, 114.2)
- added P8: PAD, footprint:PAD_0.6x1.0_SMD, F.Cu at (131.8, 101.8)
- added P8: PAD, footprint:PAD_0.6x1.0_SMD, F.Cu at (131.8, 89.2)
- added P8: PAD, footprint:PAD_0.6x1.0_SMD, F.Cu at (131.8, 76.8)
- added P8: PAD, footprint:PAD_0.6x1.0_SMD, F.Cu at (131.8, 64.2)
- added P8: PAD, footprint:PAD_0.6x1.0_SMD, F.Cu at (131.8, 51.8)
- added P9: PROG, footprint:PAD_PROG_2PIN_HOLE0.7, F.Cu at (165.1, 126.8)
- added P9: PROG, footprint:PAD_PROG_2PIN_HOLE0.7, F.Cu at (165.1, 114.2)
- added P9: PROG, footprint:PAD_PROG_2PIN_HOLE0.7, F.Cu at (165.1, 101.8)
- added P9: PROG, footprint:PAD_PROG_2PIN_HOLE0.7, F.Cu at (165.1, 89.2)
- added P9: PROG, footprint:PAD_PROG_2PIN_HOLE0.7, F.Cu at (165.1, 76.8)
- added P9: PROG, footprint:PAD_PROG_2PIN_HOLE0.7, F.Cu at (165.1, 64.2)
- added P9: PROG, footprint:PAD_PROG_2PIN_HOLE0.7, F.Cu at (165.1, 51.8)
- added Q1: DMG6601LVT, footprint:SOT-23-6, F.Cu at (144.5, 127.0)
- added Q1: DMG6601LVT, footprint:SOT-23-6, F.Cu at (144.5, 114.5)
- added Q1: DMG6601LVT, footprint:SOT-23-6, F.Cu at (144.5, 102.0)
- added Q1: DMG6601LVT, footprint:SOT-23-6, F.Cu at (144.5, 89.5)
- added Q1: DMG6601LVT, footprint:SOT-23-6, F.Cu at (144.5, 77.0)
- added Q1: DMG6601LVT, footprint:SOT-23-6, F.Cu at (144.5, 64.5)
- added Q1: DMG6601LVT, footprint:SOT-23-6, F.Cu at (144.5, 52.0)
- added Q11: SSM3K7002BFU, footprint:SC-70_v2, F.Cu at (121.2, 127.2)
- added Q11: SSM3K7002BFU, footprint:SC-70_v2, F.Cu at (121.2, 114.8)
- added Q11: SSM3K7002BFU, footprint:SC-70_v2, F.Cu at (121.2, 102.2)
- added Q11: SSM3K7002BFU, footprint:SC-70_v2, F.Cu at (121.2, 89.8)
- added Q11: SSM3K7002BFU, footprint:SC-70_v2, F.Cu at (121.2, 77.2)
- added Q11: SSM3K7002BFU, footprint:SC-70_v2, F.Cu at (121.2, 64.8)
- added Q11: SSM3K7002BFU, footprint:SC-70_v2, F.Cu at (121.2, 52.2)
- added Q12: SSM6N7002BFE, footprint:SOT-666-nomark, F.Cu at (170.1, 131.3)
- added Q12: SSM6N7002BFE, footprint:SOT-666-nomark, F.Cu at (170.1, 118.8)
- added Q12: SSM6N7002BFE, footprint:SOT-666-nomark, F.Cu at (170.1, 106.3)
- added Q12: SSM6N7002BFE, footprint:SOT-666-nomark, F.Cu at (170.1, 93.8)
- added Q12: SSM6N7002BFE, footprint:SOT-666-nomark, F.Cu at (170.1, 81.3)
- added Q12: SSM6N7002BFE, footprint:SOT-666-nomark, F.Cu at (170.1, 68.8)
- added Q12: SSM6N7002BFE, footprint:SOT-666-nomark, F.Cu at (170.1, 56.3)
- added Q13: SSM6N7002BFE, footprint:SOT-666-nomark, F.Cu at (167.6, 133.5)
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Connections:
- Q12 pad 2: Func2 -> Func4
- Q13 pad 2: Func3 -> Func5
- Q13 pad 5: Func4 -> Func3
- Q14 pad 2: Func5 -> Func6
- Q14 pad 5: Func6 -> Func2
- U2 pad 11: Func2 -> Func4
- U2 pad 13: Func8 -> DIR_JP
- U2 pad 15: Func5 -> Func6
- U2 pad 16: Func6 -> Func2
- U2 pad 8: Func4 -> Func3
- U2 pad 9: Func3 -> Func5
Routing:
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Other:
- rule pad_to_mask_clearance: 0 -> 0.05
- board text added: "K3066RA Rev.3 2021.04"
- board text added: "Rev.3 2021.04"
- board text removed: "K3066RA Rev.2 2021.03"
- board text removed: "Rev.2 2021.03"

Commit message: 基板上のF表記をP表記に変更
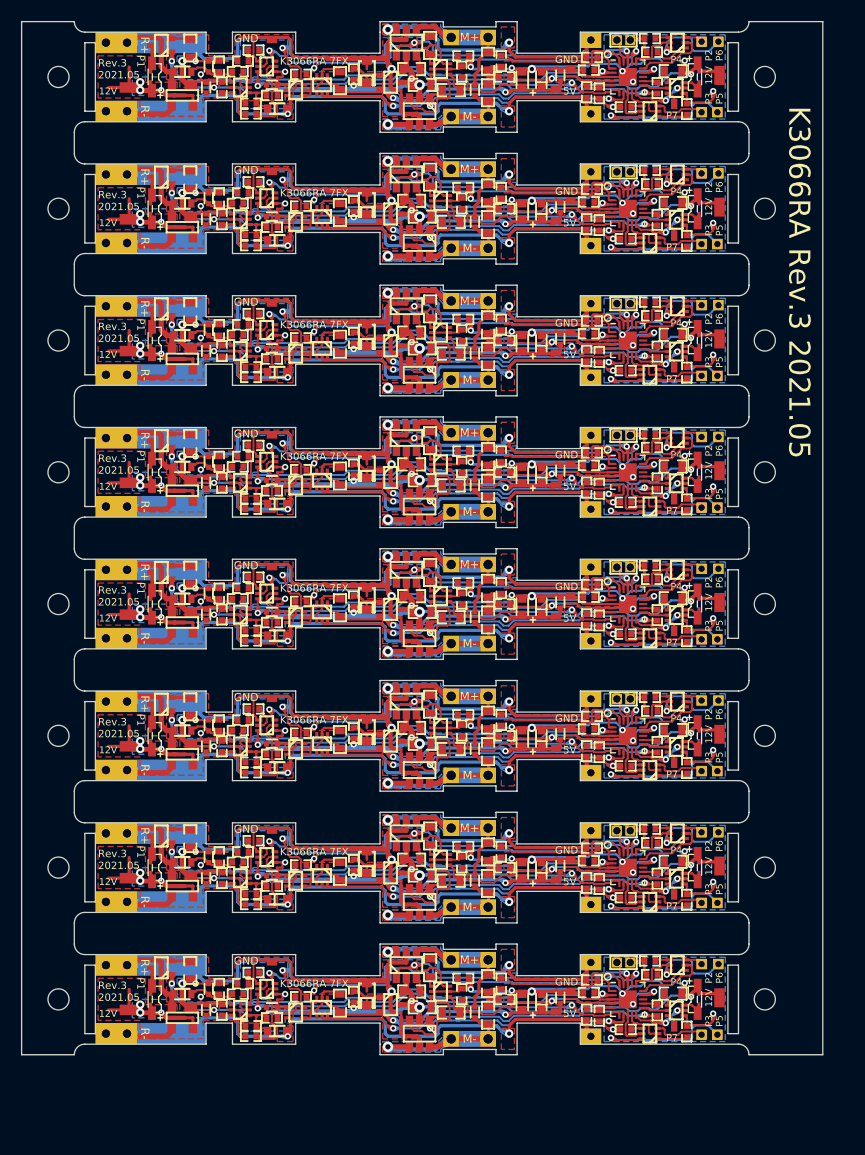
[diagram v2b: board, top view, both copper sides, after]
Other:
- board text added: "K3066RA Rev.3 2021.05"
- board text added: "P1"
- board text added: "P2"
- board text added: "P3"
- board text added: "P4"
- board text added: "P5"
- board text added: "P6"
- board text added: "P7"
- board text added: "Rev.3 2021.05"
- board text removed: "F1"
- board text removed: "F2"
- board text removed: "F3"
- board text removed: "F4"
- board text removed: "F5"
- board text removed: "F6"
- board text removed: "F7"
- board text removed: "K3066RA Rev.3 2021.04"
- board text removed: "Rev.3 2021.04"
